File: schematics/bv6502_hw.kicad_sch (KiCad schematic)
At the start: 0 parts

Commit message: new ft232h wip
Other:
- added sheet FT232H (ft232h.kicad_sch)
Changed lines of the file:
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@@
+	)
+	(sheet
+		(at 118.11 26.67)
+		(size 25.4 22.86)
+		(exclude_from_sim no)
+		(in_bom yes)
+		(on_board yes)
+		(dnp no)
+		(fields_autoplaced yes)
+		(stroke
+			(width 0.1524)
+			(type solid)
+		)
+		(fill
+			(color 0 0 0 0)
+		)
+		(property "Sheetname" "FT232H"
+			(at 118.11 25.9584 0)
+			(show_name no)
+			(do_not_autoplace no)
+			(effects
+				(font
+					(size 1.27 1.27)
+				)
+				(justify left bottom)
+			)
+		)
+		(property "Sheetfile" "ft232h.kicad_sch"
+			(at 118.11 50.1146 0)
+			(show_name no)
+			(do_not_autoplace no)
+			(effects
+				(font
+					(size 1.27 1.27)
+				)
+				(justify left top)
+			)
+		)
+		(instances
+			(project "bv6502_hw"
+				(path "/94c72abe-aaa5-49aa-8ab7-5d3e7cbc10be"
+					(page "11")
+				)
+			)
+		)
 	)
 	(sheet

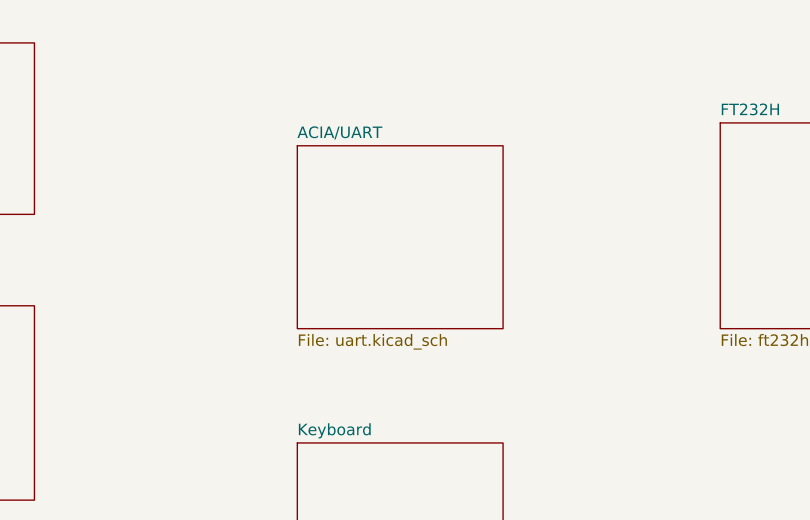
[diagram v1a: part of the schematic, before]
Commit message: new ft245 support
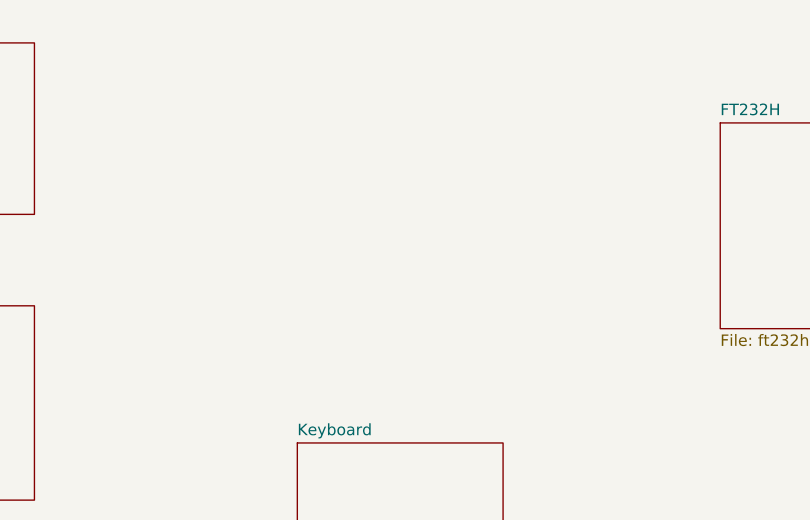
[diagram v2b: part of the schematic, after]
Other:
- removed sheet ACIA/UART
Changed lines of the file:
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@@
-	)
-	(sheet
-		(at 71.12 29.21)
-		(size 22.86 20.32)
-		(exclude_from_sim no)
-		(in_bom yes)
-		(on_board yes)
-		(dnp no)
-		(fields_autoplaced yes)
-		(stroke
-			(width 0.1524)
-			(type solid)
-		)
-		(fill
-			(color 0 0 0 0)
-		)
-		(property "Sheetname" "ACIA/UART"
-			(at 71.12 28.4984 0)
-			(show_name no)
-			(do_not_autoplace no)
-			(effects
-				(font
-					(size 1.27 1.27)
-				)
-				(justify left bottom)
-			)
-		)
-		(property "Sheetfile" "uart.kicad_sch"
-			(at 71.12 50.1146 0)
-			(show_name no)
-			(do_not_autoplace no)
-			(effects
-				(font
-					(size 1.27 1.27)
-				)
-				(justify left top)
-			)
-		)
-		(instances
-			(project "bv6502_hw"
-				(path "/94c72abe-aaa5-49aa-8ab7-5d3e7cbc10be"
-					(page "6")
-				)
-			)
-		)
 	)
 	(sheet
@@
 			(project "bv6502_hw"
 				(path "/94c72abe-aaa5-49aa-8ab7-5d3e7cbc10be"
-					(page "11")
-				)
-			)
+					(page "6")
+				)
+			)
